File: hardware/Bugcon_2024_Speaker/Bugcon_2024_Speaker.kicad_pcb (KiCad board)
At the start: 2 copper layers, 81.7 x 139.8 mm, 48 parts, among them J1 OLED, J2 Add_On, J4 Battery, J5 Battery, P1 USB_C_Plug_USB2.0, Q1 DMG3415U-7, SW1 ON, U1 ESP32-C6-WROOM-1U-N4, U2 AP2112K-3.3

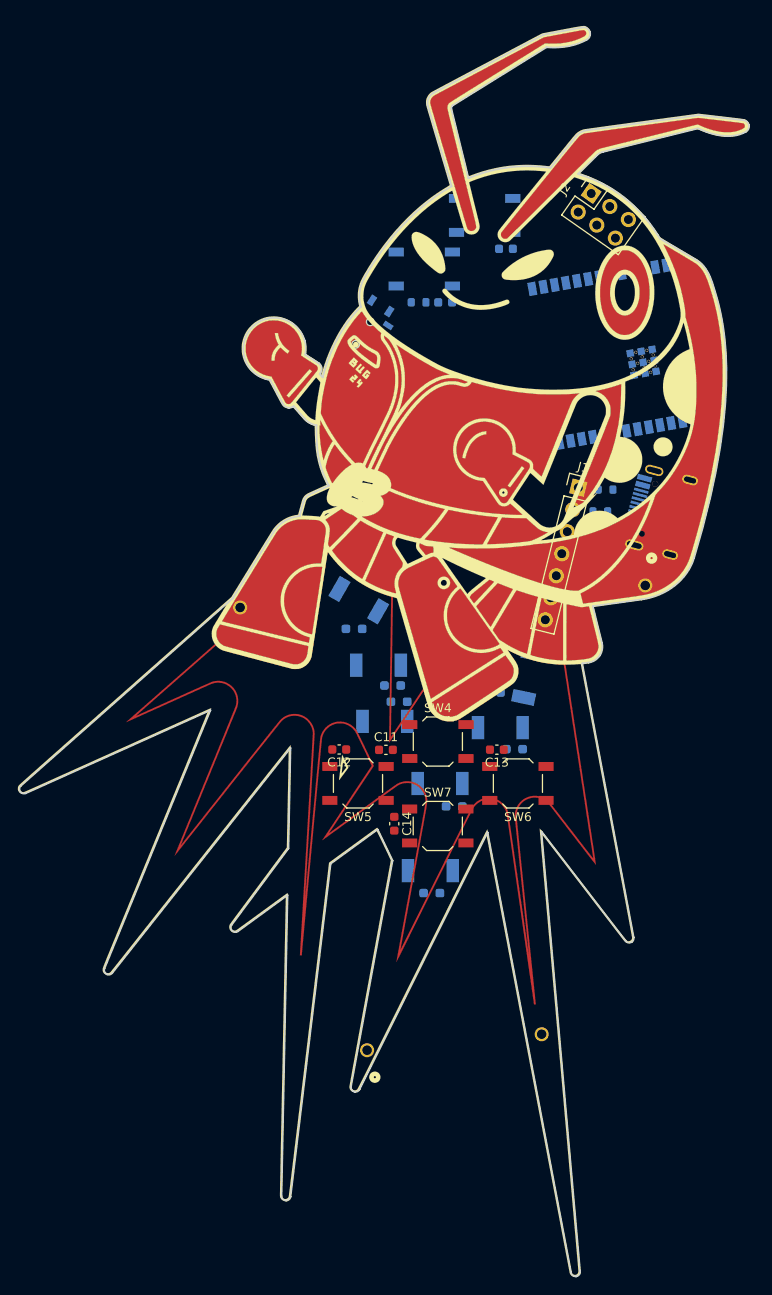
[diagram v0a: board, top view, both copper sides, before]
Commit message: feat(Hw): Update route
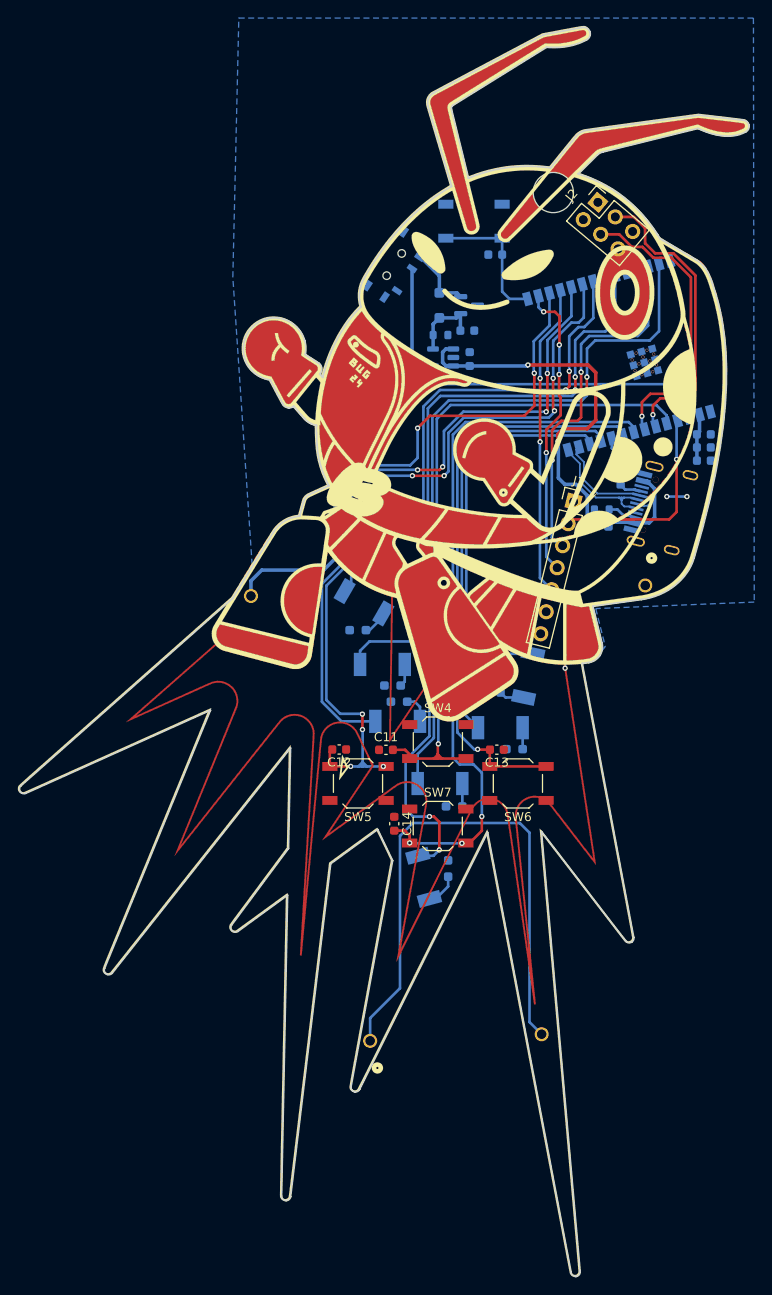
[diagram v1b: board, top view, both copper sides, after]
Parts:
- added ?: , , F.Cu at (139.3, 50.2)
- moved SW3 16.6 mm to (118.2, 74.0), turned to 0 degrees
- moved C7 13.8 mm to (115.8, 70.3), turned to 0 degrees
- moved R6 9.48 mm to (118.8, 70.3), turned to 0 degrees
- moved C1 8.63 mm to (129.9, 68.8)
- moved C2 8.63 mm to (129.7, 65.6)
- moved Q1 8.63 mm to (129.9, 62.8)
- moved D1 8.63 mm to (126.5, 62.8)
- moved R2 8.63 mm to (126.7, 66.1)
- moved U2 8.63 mm to (127.0, 68.7)
- moved SW1 8.43 mm to (121.5, 58.2), turned to 56 degrees
- moved R12 3.31 mm to (127.5, 125.8), turned to 90 degrees
- moved R3 2.15 mm to (146.8, 82.1), turned to -90 degrees
- moved J1 1.65 mm to (141.6, 84.8)
- moved D2 1.43 mm to (121.9, 109.4)
- moved C6 1.36 mm to (132.8, 57.1)
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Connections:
- D2 pad 2: /LED3 -> /LED4
- D3 pad 2: /LED4 -> /LED5
- D4 pad 2: /LED3 -> /LED6
- D5 pad 2: /LED4 -> /LED7
- D9 pad 2: /LED4 -> /LED3
- J1 pad 1: unconnected-(J1-Pin_1-Pad1) -> /RST
- J1 pad 2: unconnected-(J1-Pin_2-Pad2) -> /CS
- J1 pad 3: unconnected-(J1-Pin_3-Pad3) -> /DC
- J1 pad 4: unconnected-(J1-Pin_4-Pad4) -> /SDAO
- J1 pad 5: unconnected-(J1-Pin_5-Pad5) -> /SCLO
- J1 pad 6: unconnected-(J1-Pin_6-Pad6) -> GND
- J1 pad 7: unconnected-(J1-Pin_7-Pad7) -> /VOUT
- J2 pad 5: /GPIO3 -> unconnected-(J2-Pin_5-Pad5)
- J2 pad 6: /GPIO2 -> unconnected-(J2-Pin_6-Pad6)
- U1 pad 11: /PIN -> /LED5
- U1 pad 12: unconnected-(U1-IO11-Pad12) -> /LED1
- U1 pad 16: unconnected-(U1-IO18-Pad16) -> /SDAO
- U1 pad 17: unconnected-(U1-IO19-Pad17) -> /LED4
- U1 pad 18: unconnected-(U1-IO20-Pad18) -> /SCLO
- U1 pad 19: unconnected-(U1-IO21-Pad19) -> /LEFT
- U1 pad 20: /UP -> /LED2
- U1 pad 21: /DOWN -> /LED3
- U1 pad 23: /RIGHT -> /LED6
- U1 pad 24: /RX -> unconnected-(U1-RXD0-Pad24)
- U1 pad 25: /TX -> unconnected-(U1-TXD0-Pad25)
- U1 pad 26: /GPIO3 -> /DC
- U1 pad 27: /GPIO2 -> /LED7
- U1 pad 4: /RX1 -> /CS
- U1 pad 5: /TX1 -> /UP
- U1 pad 8: unconnected-(U1-IO40-Pad8) -> /DOWN
- U1 pad 9: /LEFT -> /RIGHT
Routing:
- net /LED6: track 0.00 -> 89.8 mm, vias 0 -> 4
- net /LEFT: track 0.00 -> 88.9 mm, vias 0 -> 8
- net /LED7: track 0.00 -> 81.8 mm, vias 0 -> 2
- net /DOWN: track 0.00 -> 79.7 mm, vias 0 -> 3
- net /UP: track 0.00 -> 76.0 mm, vias 0 -> 1
- net /LED4: track 0.00 -> 73.4 mm, vias 0 -> 2
- net /LED3: track 0.00 -> 65.4 mm, vias 0 -> 2
- net /RIGHT: track 0.00 -> 65.3 mm, vias 0 -> 1
- net Net-(J4-Pin_1): track 0.00 -> 63.0 mm
- net /LED2: track 0.00 -> 57.3 mm, vias 0 -> 4
- net /LED5: track 0.00 -> 49.6 mm
- net /EN: track 0.00 -> 47.3 mm
- net /LED1: track 0.00 -> 44.3 mm
- net VBUS: track 0.00 -> 42.8 mm, vias 0 -> 2
- net /DC: track 0.00 -> 40.7 mm, vias 0 -> 2
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- added copper zone on B.Cu, net GND
- added copper zone on F.Cu, net GND

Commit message: feat(Hw): Update route
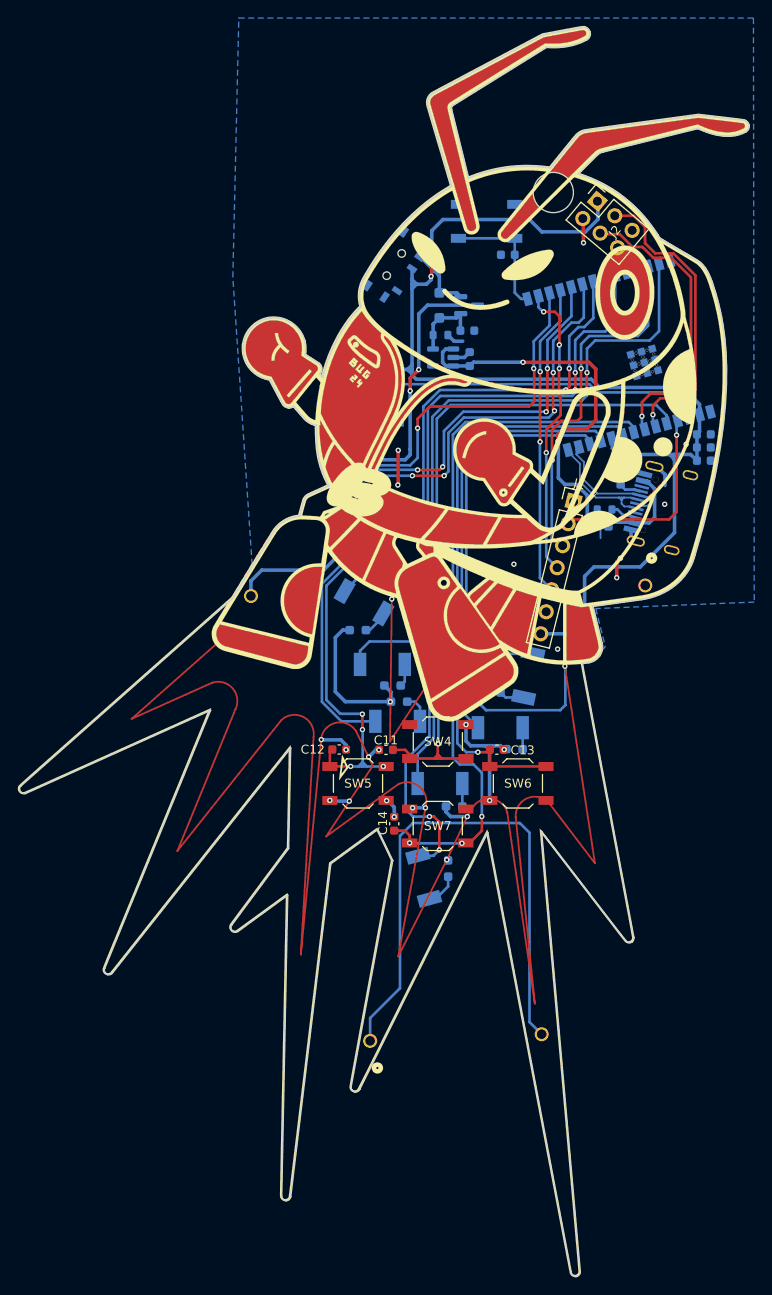
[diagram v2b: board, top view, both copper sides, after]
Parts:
- moved C6 1.41 mm to (134.2, 57.2)
- moved SW2 1.41 mm to (131.8, 53.4)
- moved SW3 0.39 mm to (118.5, 74.0)
- moved R4 0.31 mm to (145.0, 85.7)
- moved J2 0.14 mm to (144.2, 51.2)
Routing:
- net GND: track 3.76 -> 351.7 mm, vias 3 -> 27
- net /VOUT: track 20.0 -> 129.4 mm, vias 0 -> 2
- net +BATT: track 22.1 -> 54.1 mm, vias 0 -> 2
- net /BOOT: track 15.5 -> 14.1 mm
- net /RIGHT: track 65.3 -> 66.2 mm
- net /EN: track 47.3 -> 46.6 mm
- net VBUS: track 42.8 -> 43.3 mm

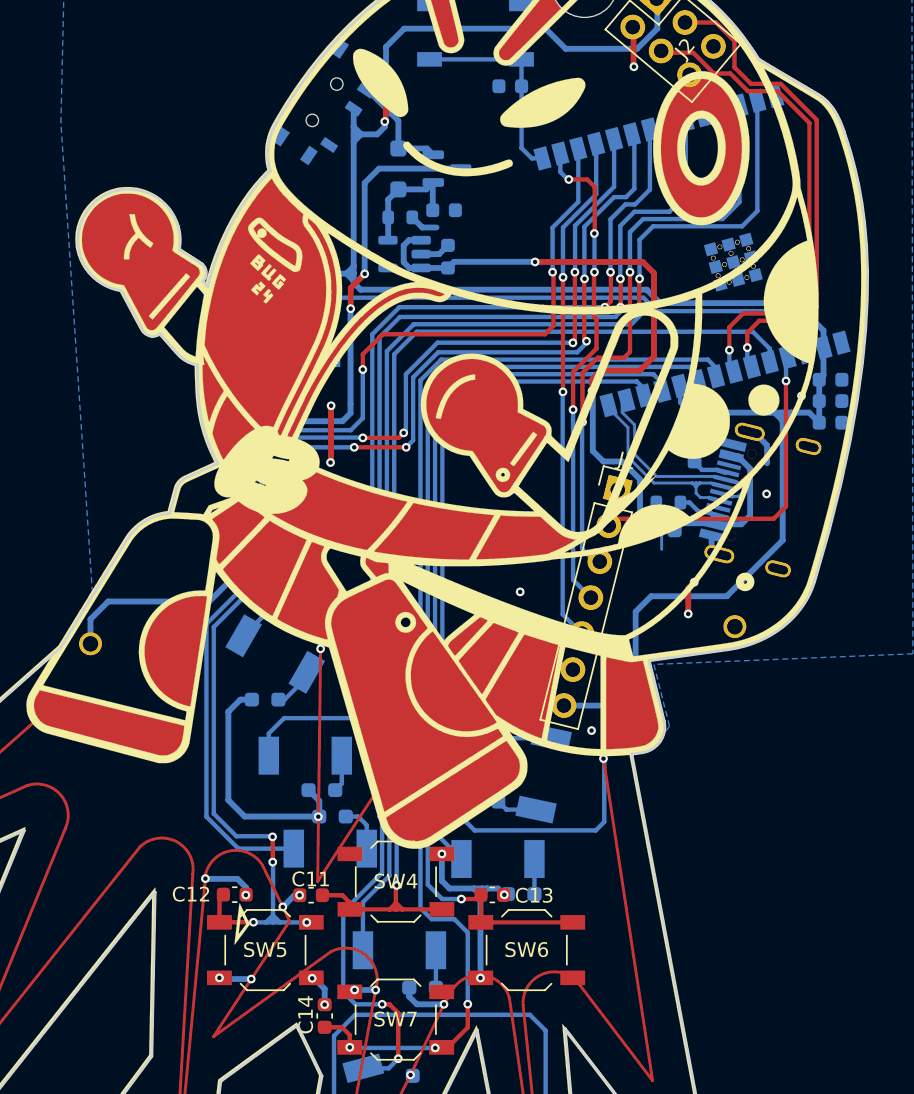
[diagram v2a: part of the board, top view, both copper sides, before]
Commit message: feat(Hw):Connected_Reset_Update_Regulator
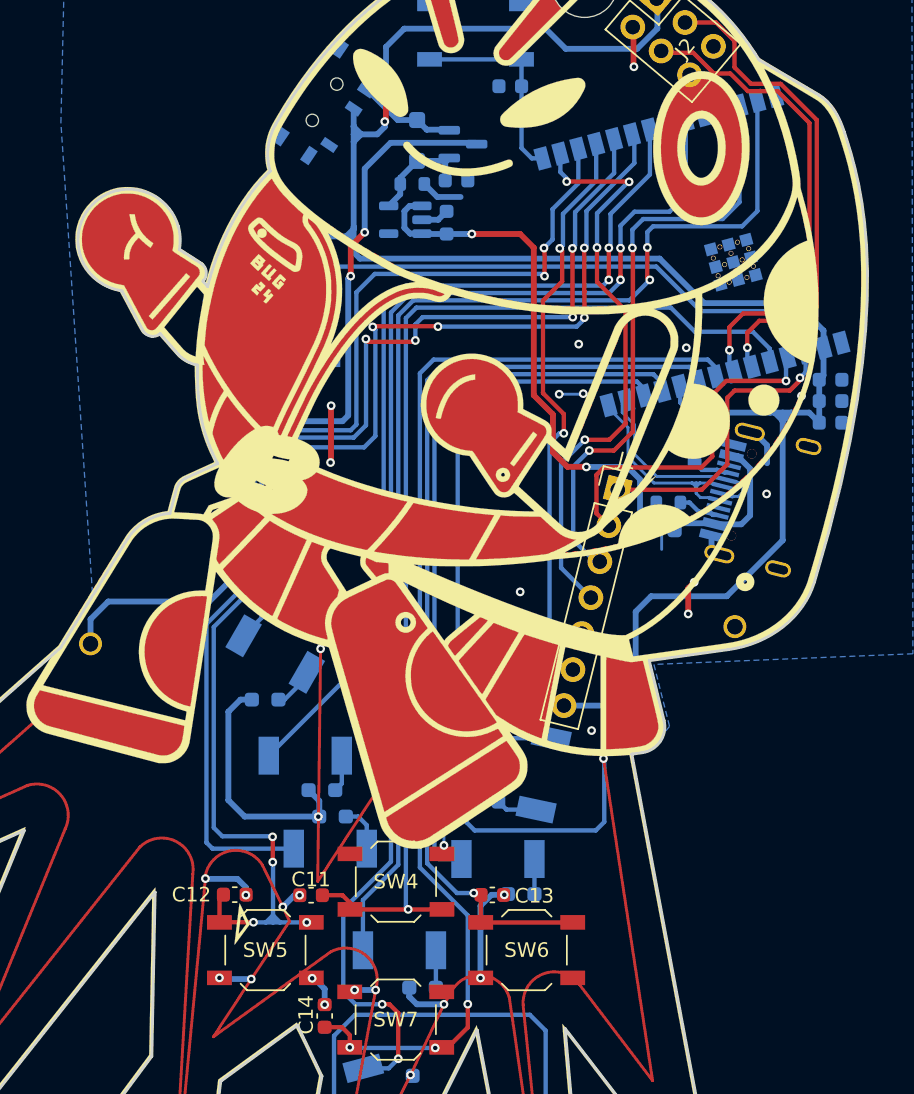
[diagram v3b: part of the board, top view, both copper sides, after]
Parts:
- moved R2 2.43 mm to (127.5, 63.9)
- moved U2 2.35 mm to (127.0, 66.3)
- moved D1 2.34 mm to (127.8, 60.9)
- moved C1 2.33 mm to (129.8, 66.5)
- moved C2 2.21 mm to (130.5, 63.6)
- moved Q1 2.00 mm to (130.9, 61.1)
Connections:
- J1 pad 1: /RST -> /EN
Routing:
- net /EN: track 46.6 -> 70.0 mm, vias 0 -> 1
- net /SDAO: track 33.4 -> 40.3 mm
- net VBUS: track 43.3 -> 36.7 mm
- net /LED3: track 65.4 -> 61.6 mm
- net /SCLO: track 35.0 -> 38.1 mm
- net +BATT: track 54.1 -> 56.5 mm
- net GND: track 351.7 -> 350.2 mm, vias 27 -> 31
- net /LED4: track 73.3 -> 74.9 mm
- net /LEFT: track 88.5 -> 90.0 mm
- net /LED1: track 44.3 -> 42.9 mm
- net /LED5: track 49.6 -> 50.7 mm
- net /VOUT: track 129.4 -> 130.3 mm
- net /LED6: track 89.8 -> 89.0 mm
- net /RIGHT: track 66.2 -> 65.4 mm
- net Net-(D1-K): track 7.55 -> 6.84 mm
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
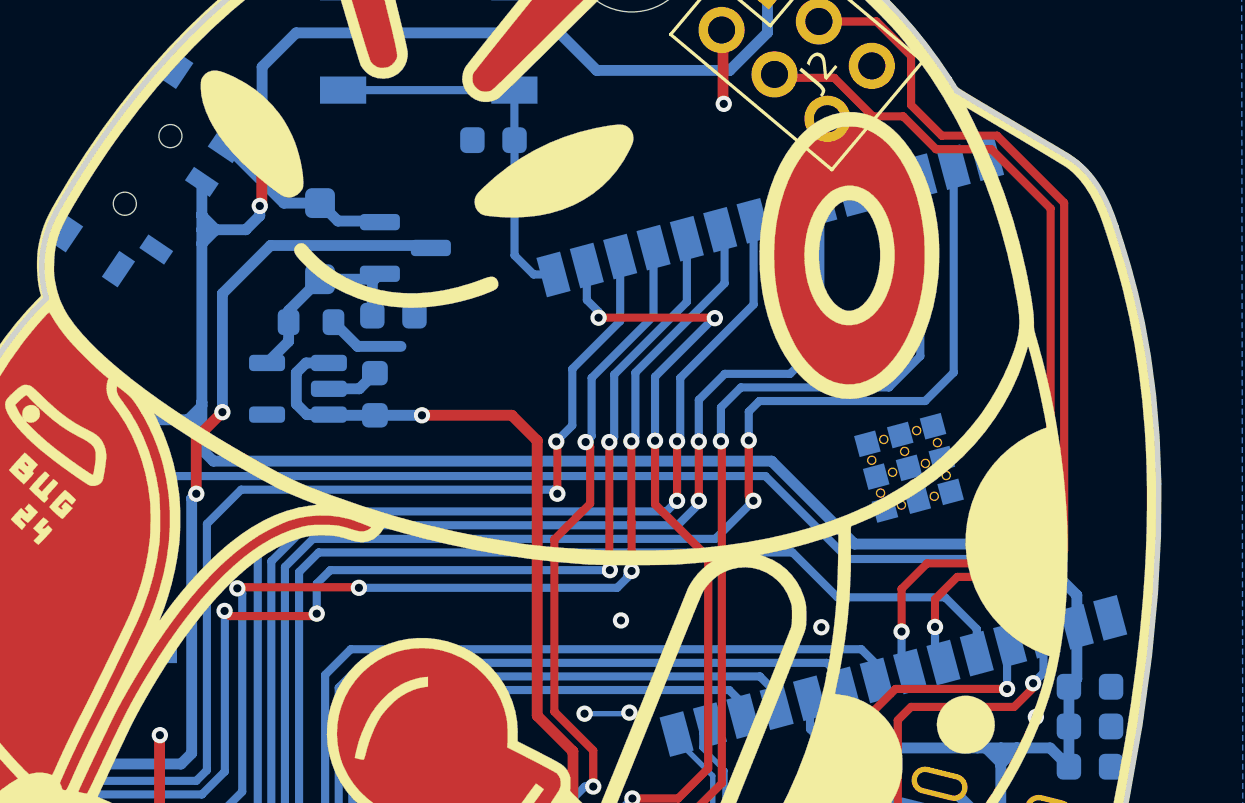
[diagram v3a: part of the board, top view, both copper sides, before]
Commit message: feat(Hw): Update ground areas
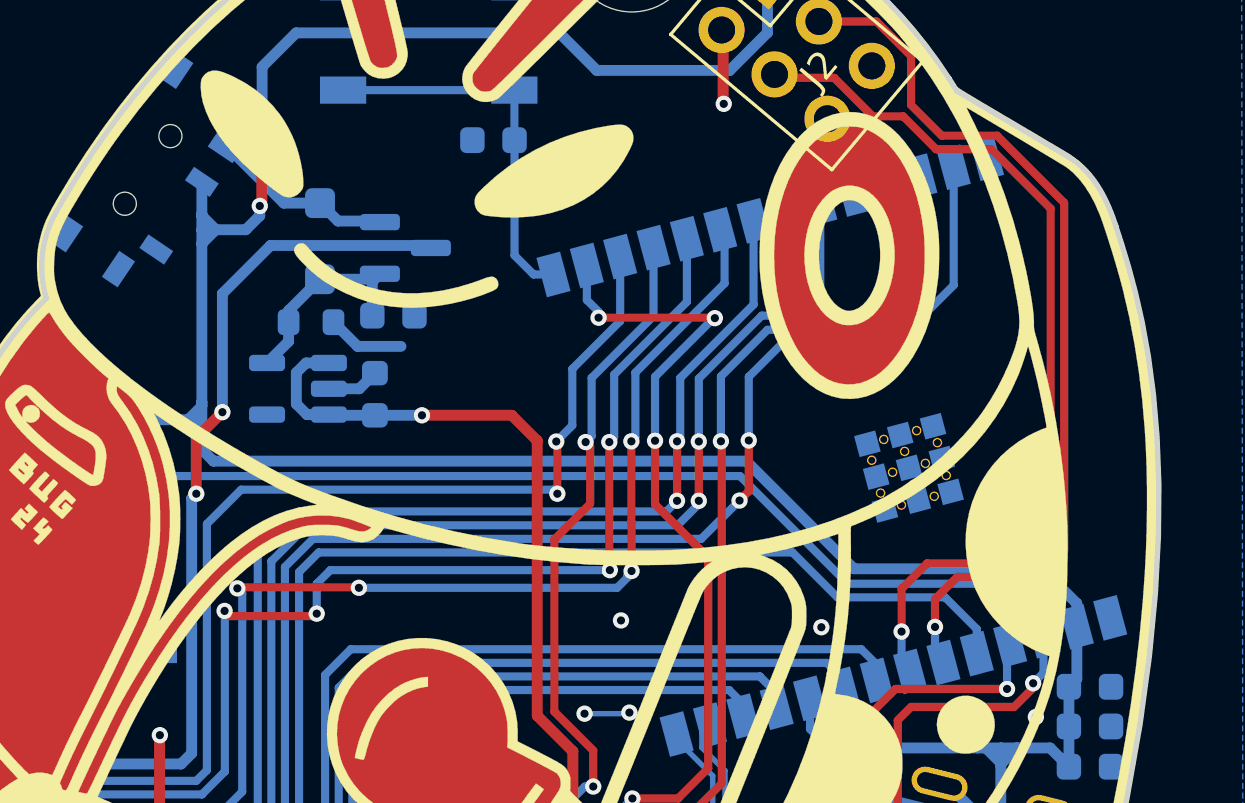
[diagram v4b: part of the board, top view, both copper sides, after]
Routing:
- net /LED7: track 81.8 -> 80.2 mm
- net /EN: track 70.0 -> 69.3 mm
- net /DC: track 41.1 -> 40.6 mm
